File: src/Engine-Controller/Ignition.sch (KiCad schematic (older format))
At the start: 9 parts, among them P8 Solid Prop Cont, Q1 QS5U17TR

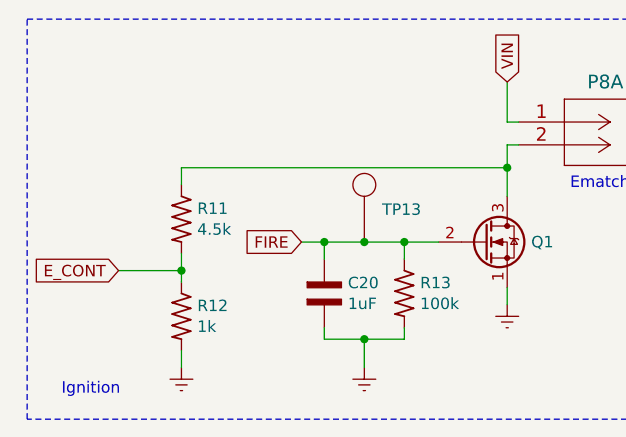
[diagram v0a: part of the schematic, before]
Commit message: Add Internal regulator stability caps
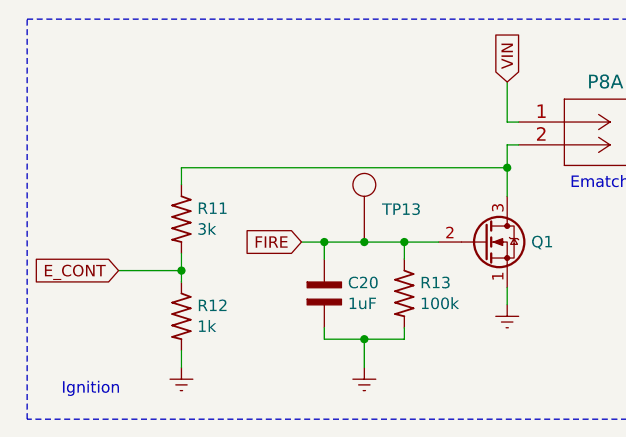
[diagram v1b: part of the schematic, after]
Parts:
- R11: value 4.5k -> 3k
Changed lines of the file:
@@
 P 3475 3700
 F 0 "R11" V 3429 3769 50  0000 L CNN
-F 1 "4.5k" V 3520 3769 50  0000 L CNN
+F 1 "3k" V 3520 3769 50  0000 L CNN
 F 2 "" H 3525 3200 50  0001 L BNN
 F 3 "" H 3475 3700 50  0001 L BNN

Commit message: finished routing rev3.0
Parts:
- C20: footprint (none) -> Engine-Controller:CAP_0603
- P8: footprint 66953-005LF_AMP -> Engine-Controller:TE_282837-6
- Q1: footprint Package_TO_SOT_THT:TO-92_Inline -> Engine-Controller:QS5U17TR
- R11, R12, R13, R14, R15: footprint (none) -> Engine-Controller:RES_0603
- TP13: footprint (none) -> Engine-Controller:TP
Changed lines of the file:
@@
 F 0 "R13" V 4404 4094 50  0000 L CNN
 F 1 "100k" V 4495 4094 50  0000 L CNN
-F 2 "" H 4500 3525 50  0001 L BNN
+F 2 "Engine-Controller:RES_0603" H 4500 3525 50  0001 L BNN
 F 3 "" H 4450 4025 50  0001 L BNN
 	1    4450 4025
@@
 F 0 "R15" V 7104 3219 50  0000 L CNN
 F 1 "10k" V 7195 3219 50  0000 L CNN
-F 2 "" H 7200 2650 50  0001 L BNN
+F 2 "Engine-Controller:RES_0603" H 7200 2650 50  0001 L BNN
 F 3 "" H 7150 3150 50  0001 L BNN
 	1    7150 3150
@@
 F 0 "R14" V 6854 3619 50  0000 L CNN
 F 1 "10k" V 6945 3619 50  0000 L CNN
-F 2 "" H 6950 3050 50  0001 L BNN
+F 2 "Engine-Controller:RES_0603" H 6950 3050 50  0001 L BNN
 F 3 "" H 6900 3550 50  0001 L BNN
 	1    6900 3550
@@
 F 0 "R12" V 3429 4194 50  0000 L CNN
 F 1 "1k" V 3520 4194 50  0000 L CNN
-F 2 "" H 3525 3625 50  0001 L BNN
+F 2 "Engine-Controller:RES_0603" H 3525 3625 50  0001 L BNN
 F 3 "" H 3475 4125 50  0001 L BNN
 	1    3475 4125
@@
 F 0 "R11" V 3429 3769 50  0000 L CNN
 F 1 "3k" V 3520 3769 50  0000 L CNN
-F 2 "" H 3525 3200 50  0001 L BNN
+F 2 "Engine-Controller:RES_0603" H 3525 3200 50  0001 L BNN
 F 3 "" H 3475 3700 50  0001 L BNN
 	1    3475 3700
@@
 F 0 "P8" H 5250 3450 60  0000 L CNN
 F 1 "Solid Prop Cont" H 5478 3177 60  0001 L CNN
-F 2 "66953-005LF_AMP" H 5100 2075 60  0001 C CNN
+F 2 "Engine-Controller:TE_282837-6" H 5100 2075 60  0001 C CNN
 F 3 "" H 4950 3275 60  0001 C CNN
 	1    4950 3275
@@
 F 0 "P8" H 7650 3500 60  0000 L CNN
 F 1 "Solid Prop Cont" H 7903 3252 60  0001 L CNN
-F 2 "66953-005LF_AMP" H 7525 2150 60  0001 C CNN
+F 2 "Engine-Controller:TE_282837-6" H 7525 2150 60  0001 C CNN
 F 3 "" H 7375 3350 60  0001 C CNN
 	3    7375 3350
@@
 F 0 "P8" H 7650 3925 60  0000 L CNN
 F 1 "Solid Prop Cont" H 7878 3677 60  0001 L CNN
-F 2 "66953-005LF_AMP" H 7500 2575 60  0001 C CNN
+F 2 "Engine-Controller:TE_282837-6" H 7500 2575 60  0001 C CNN
 F 3 "" H 7350 3775 60  0001 C CNN
 	2    7350 3775
@@
 F 0 "Q1" H 5005 3800 50  0000 L CNN
 F 1 "QS5U17TR" H 5005 3755 50  0001 L CNN
-F 2 "Package_TO_SOT_THT:TO-92_Inline" H 5000 3725 50  0001 L CIN
+F 2 "Engine-Controller:QS5U17TR" H 5000 3725 50  0001 L CIN
 F 3 "https://www.onsemi.com/pub/Collateral/NDS7002A-D.PDF" H 4800 3800 50  0001 L CNN
 	1    4800 3800
@@
 F 0 "C20" V 4054 4128 50  0000 L CNN
 F 1 "1uF" V 4145 4128 50  0000 L CNN
-F 2 "" H 4000 3625 50  0001 L BNN
+F 2 "Engine-Controller:CAP_0603" H 4000 3625 50  0001 L BNN
 F 3 "" H 4050 4025 50  0001 L BNN
 	1    4100 4025
@@
 F 0 "TP13" H 4353 3942 50  0000 L CNN
 F 1 "TP" H 4353 3897 50  0001 L CNN
-F 2 "" H 4275 3800 50  0001 C CNN
+F 2 "Engine-Controller:TP" H 4275 3800 50  0001 C CNN
 F 3 "" H 4275 3800 50  0001 C CNN
 	1    4275 3800
